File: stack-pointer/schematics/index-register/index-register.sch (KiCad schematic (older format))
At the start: 15 parts

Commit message: updated index register symbol
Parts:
- gave numbers to parts that had none: 10
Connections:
- net ERR_NXO renamed ERR_HLO
- net NXa renamed HLa
- net NXe renamed HLe
- net NXi renamed HLi
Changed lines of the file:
@@
 $EndDescr
 $Comp
-L 74xx:74LS169 U?
+L 74xx:74LS169 U7
 U 1 1 6175A069
 P 8425 3575
-F 0 "U?" V 8150 4300 50  0000 L CNN
+F 0 "U7" V 8150 4300 50  0000 L CNN
 F 1 "74LS169" V 8425 3400 50  0000 L CNN
 F 2 "" H 8425 3575 50  0001 C CNN
@@
 $EndComp
 $Comp
-L 74xx:74LS169 U?
+L 74xx:74LS169 U5
 U 1 1 6175E21D
 P 6125 3575
-F 0 "U?" V 5850 4300 50  0000 L CNN
+F 0 "U5" V 5850 4300 50  0000 L CNN
 F 1 "74LS169" V 6125 3400 50  0000 L CNN
 F 2 "" H 6125 3575 50  0001 C CNN
@@
 $EndComp
 $Comp
-L 74xx:74LS169 U?
+L 74xx:74LS169 U3
 U 1 1 61761B44
 P 3825 3575
-F 0 "U?" V 3550 4300 50  0000 L CNN
+F 0 "U3" V 3550 4300 50  0000 L CNN
 F 1 "74LS169" V 3825 3400 50  0000 L CNN
 F 2 "" H 3825 3575 50  0001 C CNN
@@
 $EndComp
 $Comp
-L 74xx:74LS169 U?
+L 74xx:74LS169 U2
 U 1 1 617638DF
 P 1525 3575
-F 0 "U?" V 1250 4300 50  0000 L CNN
+F 0 "U2" V 1250 4300 50  0000 L CNN
 F 1 "74LS169" V 1525 3400 50  0000 L CNN
 F 2 "" H 1525 3575 50  0001 C CNN
@@
 Connection ~ 6425 1350
 Text HLabel 10575 575  2    50   Input ~ 0
-NXi
-$Comp
-L 74xx:74LS04 U?
+HLi
+$Comp
+L 74xx:74LS04 U1
 U 1 1 61792AB6
 P 10100 1125
-F 0 "U?" H 10225 1000 50  0000 C CNN
+F 0 "U1" H 10225 1000 50  0000 C CNN
 F 1 "74LS04" H 10275 1250 50  0000 C CNN
 F 2 "" H 10100 1125 50  0001 C CNN
@@
 Connection ~ 3925 675
 $Comp
-L 74xx:74LS04 U?
+L 74xx:74LS04 U1
 U 2 1 6179AA95
 P 10100 2275
-F 0 "U?" H 10225 2150 50  0000 C CNN
+F 0 "U1" H 10225 2150 50  0000 C CNN
 F 1 "74LS04" H 10275 2400 50  0000 C CNN
 F 2 "" H 10100 2275 50  0001 C CNN
@@
 $EndComp
 $Comp
-L 74xx:74LS04 U?
+L 74xx:74LS04 U1
 U 3 1 617A06F8
 P 10100 2625
-F 0 "U?" H 10225 2500 50  0000 C CNN
+F 0 "U1" H 10225 2500 50  0000 C CNN
 F 1 "74LS04" H 10275 2750 50  0000 C CNN
 F 2 "" H 10100 2625 50  0001 C CNN
@@
 $EndComp
 Text HLabel 10600 2275 2    50   Input ~ 0
-NXe
+HLe
 Text HLabel 10600 2625 2    50   Input ~ 0
 SUB
@@
 	1125 2975 1125 3075
 $Comp
-L 74xx:74LS04 U?
+L 74xx:74LS04 U1
 U 4 1 617BFB3E
 P 1525 4775
-F 0 "U?" V 1475 4475 50  0000 L CNN
+F 0 "U1" V 1475 4475 50  0000 L CNN
 F 1 "74LS04" V 1575 4350 50  0000 L CNN
 F 2 "" H 1525 4775 50  0001 C CNN
@@
 Wire Wire Line
 	1525 4075 1525 4475
-Text HLabel 925  5075 0    50   Input ~ 0
-ERR_NXO
+Text HLabel 925  5075 0    50   Output ~ 0
+ERR_HLO
 Wire Wire Line
 	925  5075 1525 5075
 $Comp
-L 74xx:74LS245 U?
+L 74xx:74LS245 U4
 U 1 1 617CC3A5
 P 3925 5475
-F 0 "U?" V 3650 6100 50  0000 L CNN
+F 0 "U4" V 3650 6100 50  0000 L CNN
 F 1 "74LS245" V 3925 5525 50  0000 L CNN
 F 2 "" H 3925 5475 50  0001 C CNN
@@
 $EndComp
 $Comp
-L 74xx:74LS245 U?
+L 74xx:74LS245 U6
 U 1 1 617D2D1E
 P 6625 5475
-F 0 "U?" V 6350 6100 50  0000 L CNN
+F 0 "U6" V 6350 6100 50  0000 L CNN
 F 1 "74LS245" V 6625 5525 50  0000 L CNN
 F 2 "" H 6625 5475 50  0001 C CNN
@@
 	6425 4975 6425 4275
 $Comp
-L common-symbols:BarGraphLED_8P BAR?
+L common-symbols:BarGraphLED_8P BAR2
 U 1 1 617F6AED
 P 9675 4675
-F 0 "BAR?" H 9675 5225 50  0000 C CNN
+F 0 "BAR2" H 9675 5225 50  0000 C CNN
 F 1 "BarGraphLED_8P" H 9875 4200 50  0000 C CNN
 F 2 "" H 9675 4675 50  0001 C CNN
@@
 	4425 4075 4425 4975
 $Comp
-L common-symbols:BarGraphLED_8P BAR?
+L common-symbols:BarGraphLED_8P BAR1
 U 1 1 6184FDFC
 P 4775 4675
-F 0 "BAR?" H 4775 5225 50  0000 C CNN
+F 0 "BAR1" H 4775 5225 50  0000 C CNN
 F 1 "BarGraphLED_8P" H 4975 4225 50  0000 C CNN
 F 2 "" H 4775 4675 50  0001 C CNN
@@
 	4425 4975 4575 4975
 Text HLabel 925  5475 0    50   Input ~ 0
-NXa
-$Comp
-L 74xx:74LS04 U?
+HLa
+$Comp
+L 74xx:74LS04 U1
 U 5 1 618B4DD3
 P 1375 5475
-F 0 "U?" H 1475 5600 50  0000 C CNN
+F 0 "U1" H 1475 5600 50  0000 C CNN
 F 1 "74LS04" H 1550 5350 50  0000 C CNN
 F 2 "" H 1375 5475 50  0001 C CNN
@@
 Connection ~ 2050 5475
 $Comp
-L power:VCC #PWR?
+L power:VCC #PWR05
 U 1 1 618D1EFB
 P 3525 4975
-F 0 "#PWR?" H 3525 4825 50  0001 C CNN
+F 0 "#PWR05" H 3525 4825 50  0001 C CNN
 F 1 "VCC" H 3540 5148 50  0000 C CNN
 F 2 "" H 3525 4975 50  0001 C CNN
@@
 $EndComp
 $Comp
-L power:VCC #PWR?
+L power:VCC #PWR07
 U 1 1 618D24D7
 P 4725 5475
-F 0 "#PWR?" H 4725 5325 50  0001 C CNN
+F 0 "#PWR07" H 4725 5325 50  0001 C CNN
 F 1 "VCC" H 4740 5648 50  0000 C CNN
 F 2 "" H 4725 5475 50  0001 C CNN
@@
 $EndComp
 $Comp
-L power:VCC #PWR?
+L power:VCC #PWR010
 U 1 1 618D2AAE
 P 6225 4975
-F 0 "#PWR?" H 6225 4825 50  0001 C CNN
+F 0 "#PWR010" H 6225 4825 50  0001 C CNN
 F 1 "VCC" H 6240 5148 50  0000 C CNN
 F 2 "" H 6225 4975 50  0001 C CNN
@@
 $EndComp
 $Comp
-L power:VCC #PWR?
+L power:VCC #PWR012
 U 1 1 618D3095
 P 7425 5475
-F 0 "#PWR?" H 7425 5325 50  0001 C CNN
+F 0 "#PWR012" H 7425 5325 50  0001 C CNN
 F 1 "VCC" H 7440 5648 50  0000 C CNN
 F 2 "" H 7425 5475 50  0001 C CNN
@@
 $EndComp
 $Comp
-L power:GND #PWR?
+L power:GND #PWR09
 U 1 1 618D380F
 P 5825 5475
-F 0 "#PWR?" H 5825 5225 50  0001 C CNN
+F 0 "#PWR09" H 5825 5225 50  0001 C CNN
 F 1 "GND" H 5830 5302 50  0000 C CNN
 F 2 "" H 5825 5475 50  0001 C CNN
@@
 $EndComp
 $Comp
-L power:GND #PWR?
+L power:GND #PWR04
 U 1 1 618D3DFE
 P 3125 5475
-F 0 "#PWR?" H 3125 5225 50  0001 C CNN
+F 0 "#PWR04" H 3125 5225 50  0001 C CNN
 F 1 "GND" H 3130 5302 50  0000 C CNN
 F 2 "" H 3125 5475 50  0001 C CNN
@@
 	3725 6200 3725 5975
 $Comp
-L power:VCC #PWR?
+L power:VCC #PWR06
 U 1 1 6190F149
 P 4725 3575
-F 0 "#PWR?" H 4725 3425 50  0001 C CNN
+F 0 "#PWR06" H 4725 3425 50  0001 C CNN
 F 1 "VCC" H 4740 3748 50  0000 C CNN
 F 2 "" H 4725 3575 50  0001 C CNN
@@
 $EndComp
 $Comp
-L power:VCC #PWR?
+L power:VCC #PWR011
 U 1 1 6190FBF5
 P 7025 3575
-F 0 "#PWR?" H 7025 3425 50  0001 C CNN
+F 0 "#PWR011" H 7025 3425 50  0001 C CNN
 F 1 "VCC" H 7040 3748 50  0000 C CNN
 F 2 "" H 7025 3575 50  0001 C CNN
@@
 $EndComp
 $Comp
-L power:VCC #PWR?
+L power:VCC #PWR014
 U 1 1 619104BC
 P 9325 3575
-F 0 "#PWR?" H 9325 3425 50  0001 C CNN
+F 0 "#PWR014" H 9325 3425 50  0001 C CNN
 F 1 "VCC" H 9340 3748 50  0000 C CNN
 F 2 "" H 9325 3575 50  0001 C CNN
@@
 $EndComp
 $Comp
-L power:VCC #PWR?
+L power:VCC #PWR02
 U 1 1 61910EF1
 P 2425 3575
-F 0 "#PWR?" H 2425 3425 50  0001 C CNN
+F 0 "#PWR02" H 2425 3425 50  0001 C CNN
 F 1 "VCC" H 2440 3748 50  0000 C CNN
 F 2 "" H 2425 3575 50  0001 C CNN
@@
 $EndComp
 $Comp
-L power:GND #PWR?
+L power:GND #PWR01
 U 1 1 6191250C
 P 625 3575
-F 0 "#PWR?" H 625 3325 50  0001 C CNN
+F 0 "#PWR01" H 625 3325 50  0001 C CNN
 F 1 "GND" H 630 3402 50  0000 C CNN
 F 2 "" H 625 3575 50  0001 C CNN
@@
 $EndComp
 $Comp
-L power:GND #PWR?
+L power:GND #PWR03
 U 1 1 61912B47
 P 2925 3575
-F 0 "#PWR?" H 2925 3325 50  0001 C CNN
+F 0 "#PWR03" H 2925 3325 50  0001 C CNN
 F 1 "GND" H 2930 3402 50  0000 C CNN
 F 2 "" H 2925 3575 50  0001 C CNN
@@
 $EndComp
 $Comp
-L power:GND #PWR?
+L power:GND #PWR08
 U 1 1 619131B9
 P 5225 3575
-F 0 "#PWR?" H 5225 3325 50  0001 C CNN
+F 0 "#PWR08" H 5225 3325 50  0001 C CNN
 F 1 "GND" H 5230 3402 50  0000 C CNN
 F 2 "" H 5225 3575 50  0001 C CNN
@@
 $EndComp
 $Comp
-L power:GND #PWR?
+L power:GND #PWR013
 U 1 1 6191380C
 P 7525 3575
-F 0 "#PWR?" H 7525 3325 50  0001 C CNN
+F 0 "#PWR013" H 7525 3325 50  0001 C CNN
 F 1 "GND" H 7530 3402 50  0000 C CNN
 F 2 "" H 7525 3575 50  0001 C CNN
@@
 $EndComp
 $Comp
-L 74xx:74LS00 U?
+L 74xx:74LS00 U8
 U 1 1 6191C83E
 P 9400 675
-F 0 "U?" H 9625 550 50  0000 C CNN
+F 0 "U8" H 9625 550 50  0000 C CNN
 F 1 "74LS00" H 9700 775 50  0000 C CNN
 F 2 "" H 9400 675 50  0001 C CNN
@@
 $EndComp
 $Comp
-L 74xx:74LS00 U?
+L 74xx:74LS00 U8
 U 2 1 6191F3EE
 P 9425 1025
-F 0 "U?" H 9650 900 50  0000 C CNN
+F 0 "U8" H 9650 900 50  0000 C CNN
 F 1 "74LS00" H 9725 1125 50  0000 C CNN
 F 2 "" H 9425 1025 50  0001 C CNN

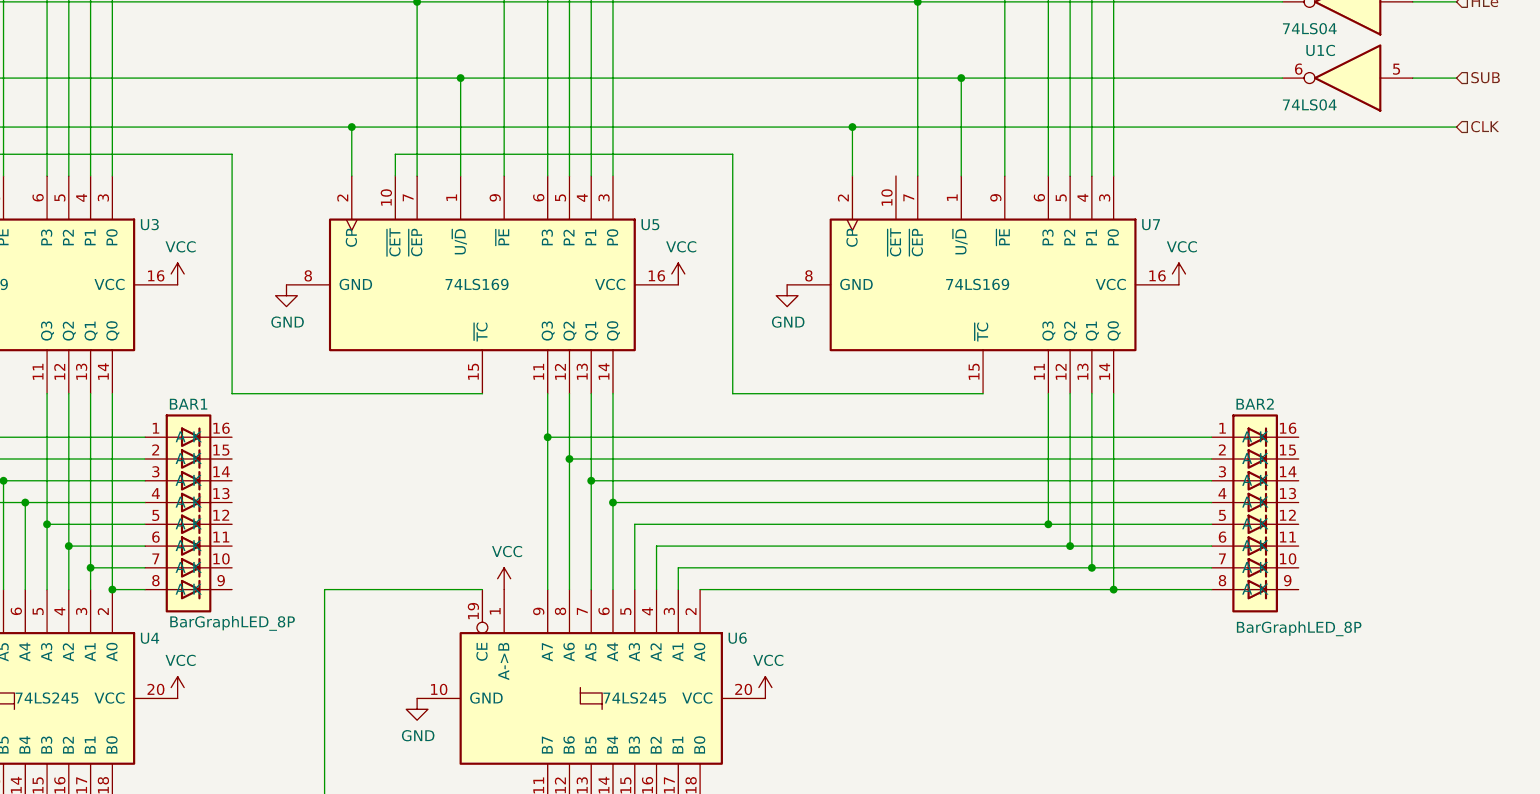
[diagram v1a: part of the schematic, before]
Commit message: finalized index register design
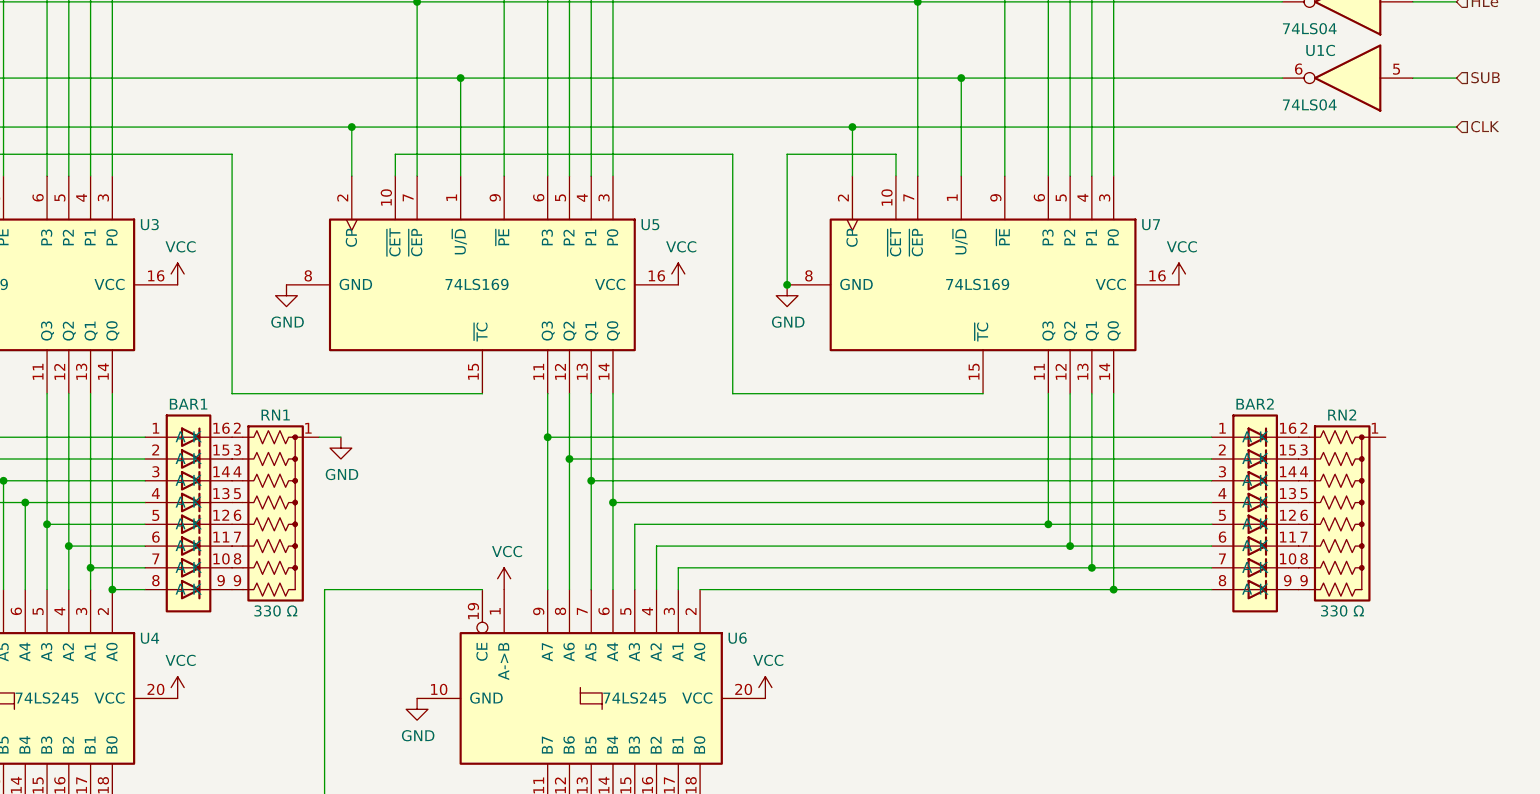
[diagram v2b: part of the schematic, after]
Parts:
- added RN1, RN2: 330 Ω, Resistor_THT:R_Array_SIP9, symbol Device:R_Network08_US
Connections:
- net GND: now also U7.10 (~CET), RN1.1 (common)
- net at BAR2.10 (K): now also RN2.8 (R7)
- net at BAR2.11 (K): now also RN2.7 (R6)
- net at BAR2.12 (K): now also RN2.6 (R5)
- net at BAR2.13 (K): now also RN2.5 (R4)
- net at BAR2.14 (K): now also RN2.4 (R3)
- net at BAR2.15 (K): now also RN2.3 (R2)
- net at BAR2.16 (K): now also RN2.2 (R1)
- net at BAR2.9 (K): now also RN2.9 (R8)
- net at BAR1.10 (K): now also RN1.8 (R7)
- net at BAR1.11 (K): now also RN1.7 (R6)
- net at BAR1.12 (K): now also RN1.6 (R5)
- net at BAR1.13 (K): now also RN1.5 (R4)
- net at BAR1.14 (K): now also RN1.4 (R3)
- net at BAR1.15 (K): now also RN1.3 (R2)
- net at BAR1.16 (K): now also RN1.2 (R1)
- net at BAR1.9 (K): now also RN1.9 (R8)
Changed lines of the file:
@@
 Rev ""
 Comp ""
-Comment1 ""
-Comment2 ""
-Comment3 ""
+Comment1 "HLi - read in from data bus to byte according to HI~LO~"
+Comment2 "HLe - increment or decrement according to SUB"
+Comment3 "HLa - write register value to address bus"
 Comment4 ""
 $EndDescr
@@
 P 9675 4675
 F 0 "BAR2" H 9675 5225 50  0000 C CNN
-F 1 "BarGraphLED_8P" H 9875 4200 50  0000 C CNN
+F 1 "BarGraphLED_8P" H 9675 4225 50  0001 C CNN
 F 2 "" H 9675 4675 50  0001 C CNN
 F 3 "" H 9675 4675 50  0001 C CNN
@@
 P 4775 4675
 F 0 "BAR1" H 4775 5225 50  0000 C CNN
-F 1 "BarGraphLED_8P" H 4975 4225 50  0000 C CNN
+F 1 "BarGraphLED_8P" H 4975 4225 50  0001 C CNN
 F 2 "" H 4775 4675 50  0001 C CNN
 F 3 "" H 4775 4675 50  0001 C CNN
@@
 	-1   0    0    1
 $EndComp
+Wire Wire Line
+	8025 3075 8025 2975
+Wire Wire Line
+	8025 2975 7525 2975
+Wire Wire Line
+	7525 2975 7525 3575
+Connection ~ 7525 3575
+$Comp
+L Device:R_Network08_US RN2
+U 1 1 619F200F
+P 10075 4675
+F 0 "RN2" V 9575 4675 50  0000 C CNN
+F 1 "330 Ω" V 10475 4675 50  0000 C CNN
+F 2 "Resistor_THT:R_Array_SIP9" V 10550 4675 50  0001 C CNN
+F 3 "http://www.vishay.com/docs/31509/csc.pdf" H 10075 4675 50  0001 C CNN
+	1    10075 4675
+	0    1    1    0
+$EndComp
+$Comp
+L Device:R_Network08_US RN1
+U 1 1 619F6D46
+P 5175 4675
+F 0 "RN1" V 4675 4675 50  0000 C CNN
+F 1 "330 Ω" V 5575 4675 50  0000 C CNN
+F 2 "Resistor_THT:R_Array_SIP9" V 5650 4675 50  0001 C CNN
+F 3 "http://www.vishay.com/docs/31509/csc.pdf" H 5175 4675 50  0001 C CNN
+	1    5175 4675
+	0    1    1    0
+$EndComp
+$Comp
+L power:GND #PWR015
+U 1 1 619F978C
+P 5475 4275
+F 0 "#PWR015" H 5475 4025 50  0001 C CNN
+F 1 "GND" H 5480 4102 50  0000 C CNN
+F 2 "" H 5475 4275 50  0001 C CNN
+F 3 "" H 5475 4275 50  0001 C CNN
+	1    5475 4275
+	1    0    0    -1
+$EndComp
+Wire Wire Line
+	5375 4275 5475 4275
 $EndSCHEMATC

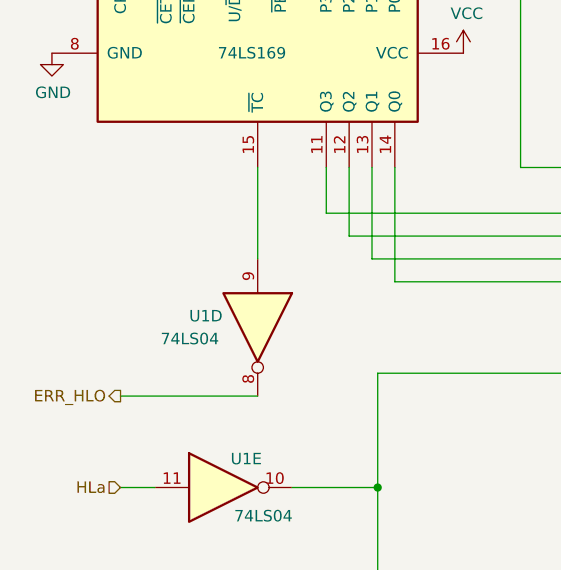
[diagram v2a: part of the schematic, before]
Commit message: removed stack pointer and index register error flags
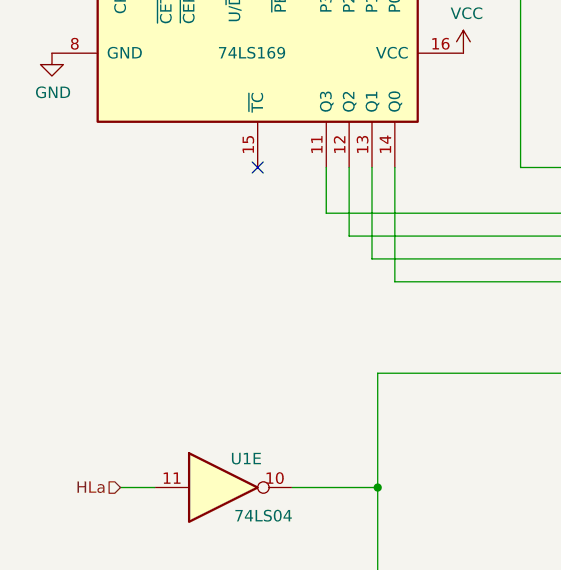
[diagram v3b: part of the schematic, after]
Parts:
- removed unit 4 of U1
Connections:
- no-connect marks 0 -> 1
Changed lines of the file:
@@
 	1125 2975 1125 3075
-$Comp
-L 74xx:74LS04 U1
-U 4 1 617BFB3E
-P 1525 4775
-F 0 "U1" V 1475 4475 50  0000 L CNN
-F 1 "74LS04" V 1575 4350 50  0000 L CNN
-F 2 "" H 1525 4775 50  0001 C CNN
-F 3 "http://www.ti.com/lit/gpn/sn74LS04" H 1525 4775 50  0001 C CNN
-	4    1525 4775
-	0    1    1    0
-$EndComp
-Wire Wire Line
-	1525 4075 1525 4475
-Text HLabel 925  5075 0    50   Output ~ 0
-ERR_HLO
-Wire Wire Line
-	925  5075 1525 5075
 $Comp
 L 74xx:74LS245 U4
@@
 Wire Wire Line
 	5375 4275 5475 4275
+NoConn ~ 1525 4075
 $EndSCHEMATC
